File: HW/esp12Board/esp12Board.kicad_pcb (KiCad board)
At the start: 2 copper layers, 50 x 50 mm, 49 parts, among them IC1 TPS54331DR, J1 Conn_01x07, J2 Conn_01x03, J3 Conn_02x05_Odd_Even, J4 Conn_01x02, J5 Conn_01x03, J6 Conn_01x03, Q1 S8050, Q2 S8050, SW1 SW_Push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

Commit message: fixes
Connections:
- Q2 pad 3: GPIO0 -> IO0
- R7 pad 1: GPIO0 -> IO0
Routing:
- net GPIO0: track 3.34 -> 0.00 mm
- net IO0: track 27.6 -> 31.0 mm

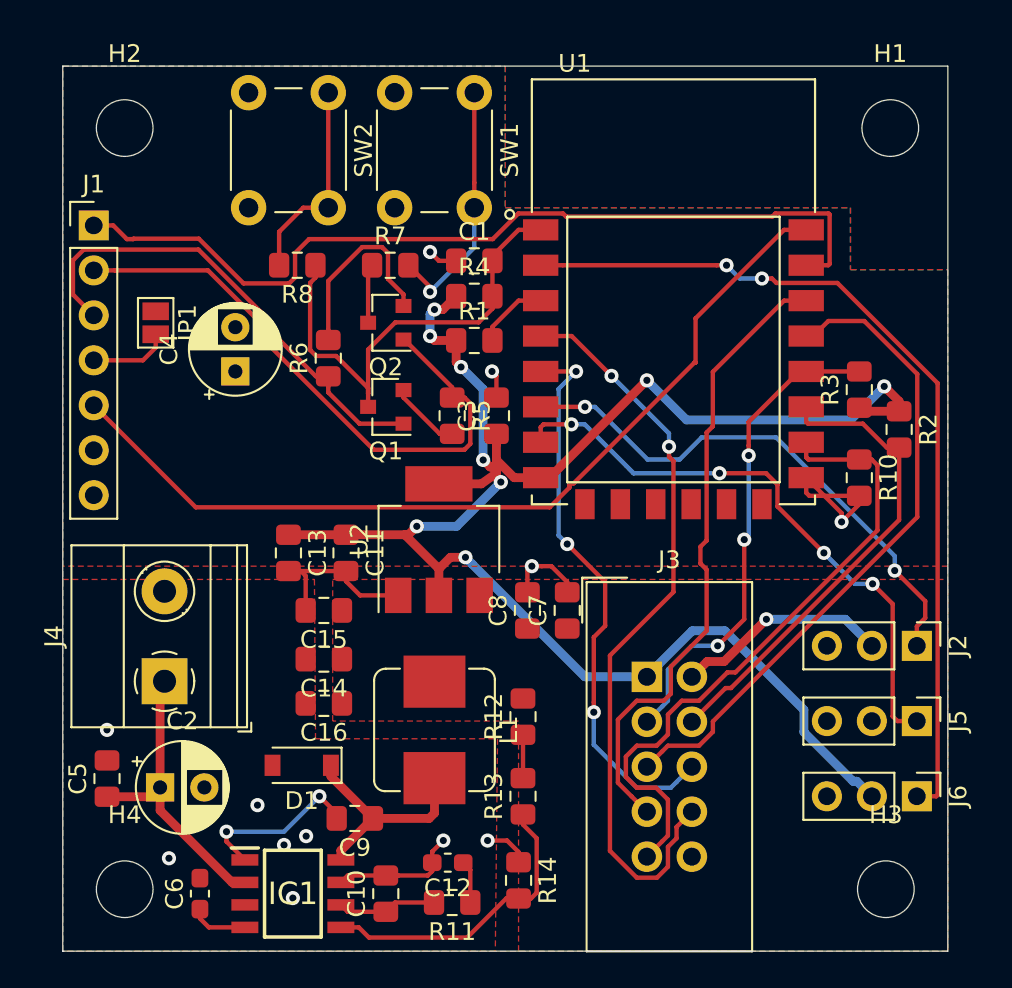
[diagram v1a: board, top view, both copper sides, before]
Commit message: Fixed npn orientation added contacts, remove boot sw
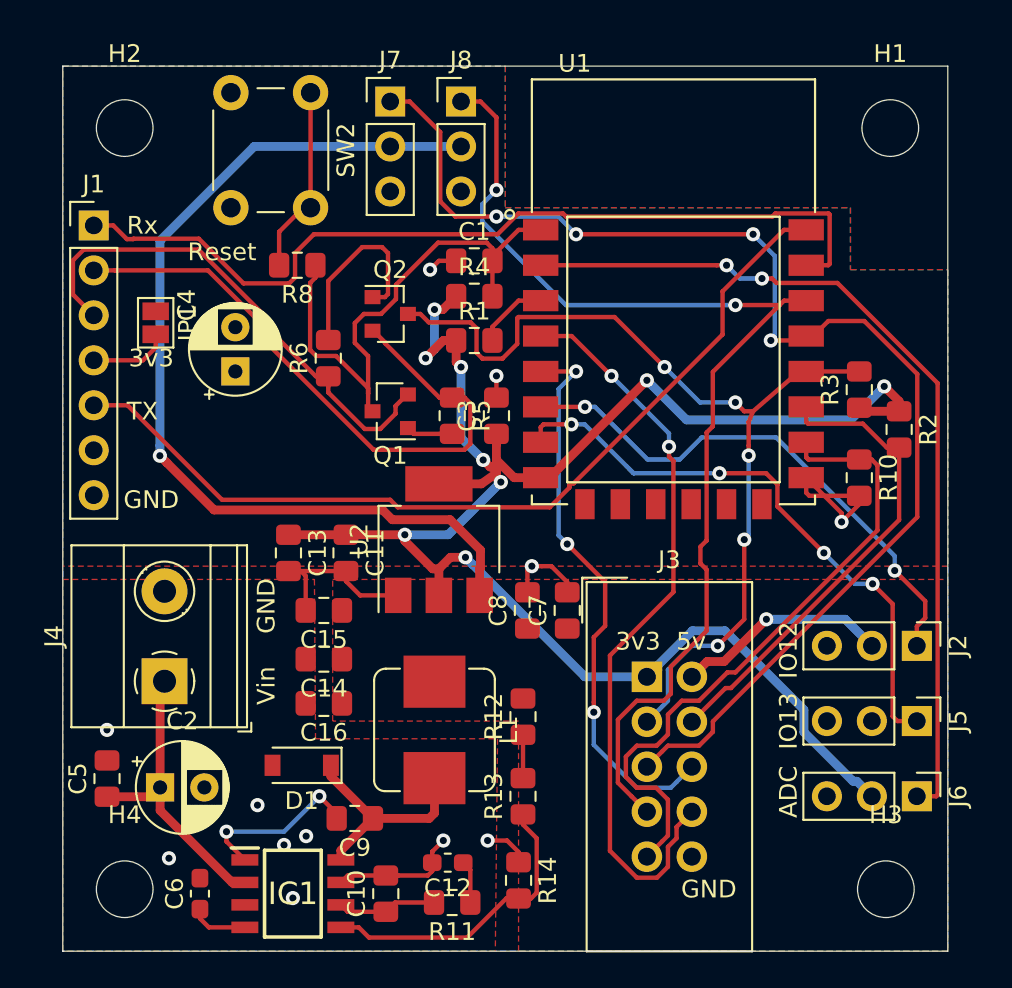
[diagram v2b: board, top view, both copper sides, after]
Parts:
- removed R7: 470, Resistor_SMD:R_0805_2012Metric_Pad1.15x1.40mm_HandSolder
- removed SW1: SW_Push, Button_Switch_THT:SW_PUSH_6mm
- added J7: Conn_01x03, Connector_PinHeader_2.54mm:PinHeader_1x03_P2.54mm_Vertical, F.Cu at (48.5, 37.0)
- added J8: Conn_01x03, Connector_PinHeader_2.54mm:PinHeader_1x03_P2.54mm_Vertical, F.Cu at (52.5, 37.0)
- Q1, Q2: value S8050 -> S8050_SMD
- moved SW2 1.00 mm to (44.0, 36.5)
- moved Q2 0.56 mm to (48.5, 49.0), turned to 0 degrees
- moved Q1 0.35 mm to (48.5, 54.5)
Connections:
- Q1 pad 1: RTS -> Net-(Q1-Pad1)
- Q1 pad 2: Net-(Q1-Pad2) -> RTS
- Q2 pad 1: DTR -> Net-(Q2-Pad1)
- Q2 pad 2: Net-(Q2-Pad2) -> DTR
- R5 pad 2: Net-(Q1-Pad2) -> Net-(Q1-Pad1)
- R6 pad 2: Net-(Q2-Pad2) -> Net-(Q2-Pad1)
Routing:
- net +5V: track 12.1 -> 66.4 mm, vias 1 -> 2
- net IO4: track 37.4 -> 72.0 mm, vias 0 -> 4
- net IO5: track 35.9 -> 63.2 mm, vias 0 -> 2
- net IO0: track 31.0 -> 53.1 mm, vias 3 -> 5
- net Net-(R7-Pad2): track 14.3 -> 0.00 mm, vias 1 -> 0
- net Net-(Q2-Pad2): track 11.0 -> 0.00 mm
- net Net-(Q2-Pad1): track 0.00 -> 10.9 mm
- net nRST: track 26.9 -> 31.0 mm
- net Net-(Q1-Pad2): track 4.02 -> 0.00 mm
- net Net-(Q1-Pad1): track 0.00 -> 3.33 mm
- net +3V3: track 101.1 -> 103.2 mm
- net RTS: track 27.4 -> 29.3 mm
- net DTR: track 34.0 -> 35.6 mm
- net Net-(R8-Pad2): track 11.7 -> 10.3 mm
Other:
- board text added: "3v3"
- board text added: "5v"
- board text added: "ADC"
- board text added: "GND"
- board text added: "IO12"
- board text added: "IO13"
- board text added: "Reset"
- board text added: "Rx"
- board text added: "TX"
- board text added: "Vin"
